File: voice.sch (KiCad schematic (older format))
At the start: 177 parts, among them U10 LM13700, U11 TA75S558F, U12 CD4053, U13 CD4053, U14 LM13700, U15 LM13700, U15 TA75S558F, U16 LM13700, U17 TL072-, U18 LM13700, U19 LM13700, U20 RC4558, U21 LM13700, U22 TS321, U23 LM13700, U24 TA75S558F

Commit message: updated values, made some notes
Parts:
- added C? (x2): 0.022μ, symbol C_US
- added Q? (x2): 2SA1832, SOT-23, symbol 2SA1832
- added Q?: 2SC4738, SOT-23, symbol 2SC4738
- added R? (x2): 47K, MyModules:SM0603-R-JRL, symbol R_US
- added R? (x2): 100K, MyModules:SM0603-R-JRL, symbol R_US
- added R?: 10K, MyModules:SM0603-R-JRL, symbol R_US
- added R?: 4.7K, MyModules:SM0603-R-JRL, symbol R_US
- added TP? (x5): TEST_POINT, symbol TEST_POINT
- R? (x3): value 470K -> 4.7meg
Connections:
- net +12V: now also Q?.2 (E), Q?.2 (E), R?.2
- net -12V: now also Q?.2 (E), R?.1, R?.1
- net ENV_SEL: now also Q?.3 (C), R?.2
- net GND: now also C?.2, C?.2
- net VCF_12dB: now also C?.1, Q?.3 (C), R?.1
- net VCF_24dB: now also C?.1, Q?.3 (C), R?.1
- net at C?.2, R?.1, R?.2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: now also TP?.1
- net at C?.2, Q?.2 (S), R?.1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: now also TP?.1
- net at Q?.2 (S), Q?.2 (S), R?.1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: now also TP?.1
- net at C?.2 (-), Q?.2 (S), Q?.2 (S)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: now also TP?.1
- net at R?.2, R?.2, R?.2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: now also TP?.1
- new net: Q?.1 (B), R?.2 (x2)
- new net: Q?.1 (B), R?.2, R?.2
- new net ENV_1/2: R?.1
- new net VCF_MODE_SEL: R?.1
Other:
- note added: "DIRECT CV"
- note added: "How does VCO1 range work?"
- note added: "MOD CONTROL CV"
- note added: "These need to be moved to module controller board"
- note removed: "MODULATION"

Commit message: added some notes about original Toshiba BJTs and FETs
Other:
- note added: "Change to Toshiba\nmatched PNP here"
- note added: "VCO1/2_MOD_SUM are mod signals\nsummed on modulatoin controller \nboard. They sum performance modulation\ncontrols as well as range for VCO2"
- note added: "VCO1_RANGE derived from two\npair of switched +10V signals.\nSee 'RANGE CV DAC' section of\nmodule controller schematic"
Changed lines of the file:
@@
 Wire Notes Line
 	19100 21200 19100 18150
+Text Notes 4725 17225 0    60   ~ 0
+VCO1_RANGE derived from two\npair of switched +10V signals.\nSee 'RANGE CV DAC' section of\nmodule controller schematic
+Text GLabel 4775 6650 0    60   Input ~ 0
+VCO1_MOD_SUM
+Text GLabel 4775 6800 0    60   Input ~ 0
+VCO2_MOD_SUM
+Text Notes 3250 7250 0    60   ~ 0
+VCO1/2_MOD_SUM are mod signals\nsummed on modulatoin controller \nboard. They sum performance modulation\ncontrols as well as range for VCO2
+Text Notes 15850 16700 2    100  ~ 0
+Change to Toshiba\nmatched PNP here
+Text Notes 22975 16150 0    60   ~ 0
+Probably need to use a lower Vgs(off) FET\nthan J112 here as in VCF envelope modulation\nselector circuit.
 $EndSCHEMATC

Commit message: changing transistor matched pairs
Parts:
- removed Q?: BC857BS, MyModules:SOT363-JRL, symbol BCM857BS
- added Q? (x2): PMP5201G, TO_SOT_Packages_SMD:SOT-353_SC-70-5, symbol PMP5201G
- Q? (x2): value J201 -> 2SK208-GR
- Q?: value J201 -> TF412S
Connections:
- net GND: now also Q?.3 (B)
- net Iabc: now also Q?.5 (C)
- net at R?.1, R?.2, TP?.1: now also Q?.1 (B)
- net at R?.1: now also Q?.2 (E), Q?.2 (E)
- net at C?.2, R?.1, U22.4 (-): now also Q?.4 (C)
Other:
- note added: "All modulation CVs are from 8 bit DAC. All are 0-5V except \nenvelope sustains. Filter cutoff is 8 bit 0-5V, scaled to 0-10V\nat a later summing node. All pitch CVS are from 14 bit DAC\nand use 0-10V"
- note added: "Probably need to use a lower Vgs(off) FET\nthan J112 here as in VCF envelope modulation\nselector circuit. Try 2SK208 - SMT 2SK30 equivalnet.\nShould be good to +/- 8V"
- note removed: "Change to Toshiba\nmatched PNP here"

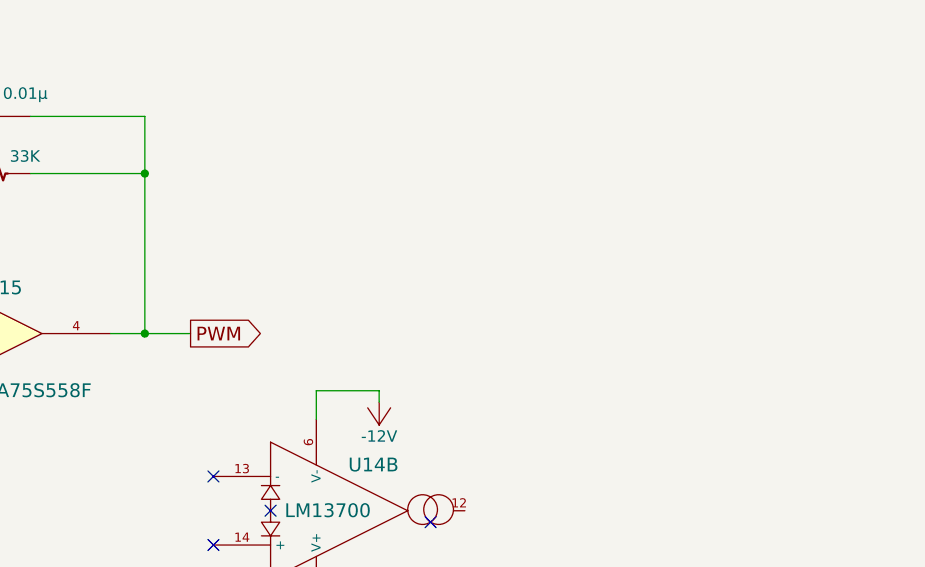
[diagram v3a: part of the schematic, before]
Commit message: more transistor fiddling
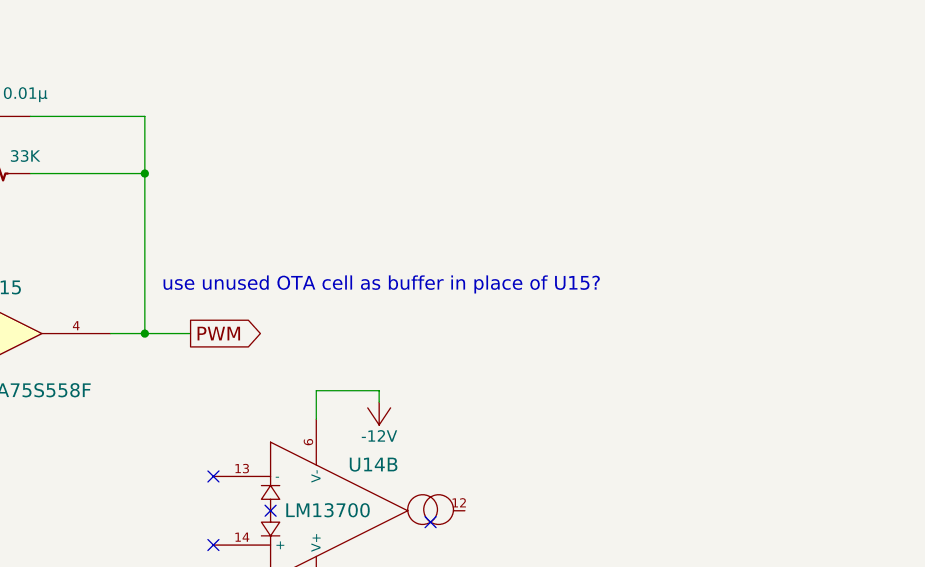
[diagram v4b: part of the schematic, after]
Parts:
- Q?: footprint MyModules:SOT23-132-JRL -> MyModules:SOT-883(XDFN3)
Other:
- note added: "use unused OTA cell as buffer in place of U15?"
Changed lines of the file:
@@
 F 0 "Q?" V 14075 20175 50  0000 R CNN
 F 1 "TF412S" V 13975 20200 50  0000 R CNN
-F 2 "MyModules:SOT23-132-JRL" H 13950 20125 29  0001 C CNN
+F 2 "MyModules:SOT-883(XDFN3)" H 13950 20125 29  0001 C CNN
 F 3 "" H 13750 20025 60  0000 C CNN
 	1    13750 20025
@@
 	-1   0    0    -1
 $EndComp
+Text Notes 19925 7475 0    60   ~ 0
+use unused OTA cell as buffer in place of U15?
 $EndSCHEMATC

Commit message: changing up NJFETS
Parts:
- removed Q? (x5): J112, MyModules:SOT23-132-JRL, symbol Q_NJFET_DSG
- removed Q? (x2): 2SK208-GR, MyModules:SOT23-132-JRL, symbol Q_NJFET_DSG
- removed Q?: TF412S, MyModules:SOT-883(XDFN3), symbol Q_NJFET_DSG
- added Q? (x7): 2SK208-GR, TO_SOT_Packages_SMD:SC-59, symbol Q_NJFET_DSG
- added Q?: 2SK932, TO_SOT_Packages_SMD:SC-59, symbol Q_NJFET_DSG
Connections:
- net +12V: now also Q?.2 (S), Q?.2 (S), Q?.2 (S), Q?.2 (S), Q?.2 (S)
- net ENV_1: now also Q?.1 (D)
- net GND: now also R?.1
- net at C?.1, U16.5: now also Q?.3 (G)
- net at C?.2, R?.1, R?.2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: now also Q?.1 (D)
- net at R?.2: now also Q?.2 (S)
- net at D?.2 (A), R?.1: now also Q?.3 (G) (x3)
- net at C?.1, U18.5: now also Q?.3 (G)
- net at R?.1, R?.2, R?.2: now also Q?.1 (D) (x2)
- net at C?.1, U18.12: now also Q?.3 (G)
- net at R?.1, R?.2, R?.2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: now also Q?.1 (D), Q?.2 (S)
- net at C?.1, U19.12: now also Q?.3 (G)
- net at C?.1, U19.5: now also Q?.3 (G)
- net at C?.2 (-), R?.1, R?.2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: now also Q?.1 (D), Q?.2 (S)
- net at C?.1 (+): now also Q?.1 (D); no longer R?.1 (x2)
- net at C?.2 (-): now also R?.1 (x2)
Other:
- note added: "Probably need to use a lower Vgs(off) FET\nthan J112 here as in VCF envelope modulation\nselector circuit. Try 2SK208 - SMT 2SK30\nequivalent. Should be good to +/- 8V"
- note removed: "Probably need to use a lower Vgs(off) FET\nthan J112 here as in VCF envelope modulation\nselector circuit."
- note removed: "Probably need to use a lower Vgs(off) FET\nthan J112 here as in VCF envelope modulation\nselector circuit. Try 2SK208 - SMT 2SK30 equivalnet.\nShould be good to +/- 8V"

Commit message: litte bit of work again - added tri sym CVs
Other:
- note added: "CHECK FOOTPRINT!"
- note added: "TRI SYM CVs may no\nbe necessary. Bipolar?"

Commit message: more voice work
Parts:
- removed C? (x2): 0.022μ, symbol C_US
- removed Q? (x2): 2SA1832, SOT-23, symbol 2SA1832
- removed Q?: 2SC4738, SOT-23, symbol 2SC4738
- removed R? (x2): 47K, MyModules:SM0603-R-JRL, symbol R_US
- removed R? (x2): 100K, MyModules:SM0603-R-JRL, symbol R_US
- removed R?: 10K, MyModules:SM0603-R-JRL, symbol R_US
- removed R?: 4.7K, MyModules:SM0603-R-JRL, symbol R_US
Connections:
- net +12V: no longer R?.2
- net ENV_1: now also R?.1
- net ENV: no longer names the net of R?.1, R?.1, R?.2, TP?.1, U21.3 (+)
- net ENV: no longer R?.1
- new net +10V: R?.2
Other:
- note added: "But 2SK932 has Vgs(max) of 15V - not good\n"
- note added: "These are generated by \n10V signals on MCB"
- note added: "VCO1_RANGE is only 4 values:\n6, 5, 4 or 3 V"
- note removed: "CHECK FOOTPRINT!"
- note removed: "These need to be moved to module controller board"
- note removed: "Toshiba TA75S558F seems like\nSC74A/SOT573 single equivalent\nto RC4558"

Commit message: added DDR3 240 connector, starting to connect input and output labels
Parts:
- added J?: DDR3-DIMM, MyModules:DDR3-DIMM-MO-269-mask-fix, symbol DDR3-DIMM
- Q?: footprint TO_SOT_Packages_SMD:SC-59 -> MyModules:SOT23-132-JRL
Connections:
- net +12V: now also J?.104, J?.18, J?.3, J?.38, J?.52, J?.62, J?.77, J?.88
- net -12V: now also J?.106, J?.20, J?.40, J?.5, J?.54, J?.64, J?.79, J?.90
- net ENV1_A: now also J?.95
- net ENV1_D: now also J?.96
- net ENV1_POL: now also J?.92
- net ENV1_R: now also J?.98
- net ENV1_S: now also J?.97
- net ENV2_A: now also J?.99
- net ENV2_D: now also J?.100
- net ENV2_R: now also J?.102
- net ENV2_S: now also J?.101
- net ENV_SEL: now also J?.73
- net GATE: now also J?.93
- net GND: now also J?.1, J?.103, J?.105, J?.107, J?.11, J?.13, J?.17, J?.19, J?.2, J?.21, J?.27, J?.35, J?.39, J?.4, J?.41, J?.43, J?.46, J?.48, J?.51, J?.53, J?.55, J?.57, J?.6, J?.61, J?.63, J?.65, J?.67, J?.72, J?.76, J?.78, J?.8, J?.80, J?.82, J?.85, J?.87, J?.89, J?.91, J?.94
- net HPF: now also J?.60
- net KCV_1: now also J?.7
- net KCV_2: now also J?.42
- net LEVEL: now also J?.84
- net LFO: now also J?.56
- net NOISE: now also J?.22
- net OUT: now also J?.86
- net PW/PWM: now also J?.26
- net PWM_LEVEL: now also J?.28
- net PWM_SEL: now also J?.25
- net RES_CTRL: now also J?.81
- net SYNC_CTRL: now also J?.14
- net VCA_BAL: now also J?.83
- net VCF_12dB: now also J?.74
- net VCF_24dB: now also J?.75
- net VCF_CUTOFF: now also J?.70
- net VCF_ENV_MOD: now also J?.71
- net VCF_KF: now also J?.68
- net VCF_TUNE: now also J?.69
- net VCO1_AUTOTUNE: now also J?.12
- net VCO1_LEVEL: now also J?.58
- net VCO1_MOD_SUM: now also J?.9
- net VCO1_MOD_SW: now also J?.23, J?.36
- net VCO1_RANGE: now also J?.66
- net VCO1_TRI_SYM: now also J?.10
- net VCO1_WF-0: now also J?.15, J?.49
- net VCO1_WF-1: now also J?.16, J?.50
- net VCO2_AUTOTUNE: now also J?.47
- net VCO2_LEVEL: now also J?.59
- net VCO2_MOD_SUM: now also J?.44
- net VCO2_MOD_SW: now also J?.24, J?.37
- net VCO2_TRI_SYM: now also J?.45
- net VCO_ENV_MOD: now also J?.31
- net VCO_ENV_MOD_BAL: now also J?.32
- net VCO_LFO_MOD: now also J?.33
- net VCO_MOD_BAL: now also J?.34
- new net CROSS_MOD: J?.29
- new net CROSS_MOD_BAL: J?.30
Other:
- note added: "NO OFFSET BALANCE HERE?"
- note removed: "How does VCO1 range work?"
- moved on the sheet: C?, Q?, R?, TP?, U15A, U15B, U16A, U17A, U17B
